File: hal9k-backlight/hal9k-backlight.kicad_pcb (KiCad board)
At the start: 2 copper layers, 76 x 13 mm, 14 parts, among them J1 +, J2 GND, J3 Din, J4 Dout

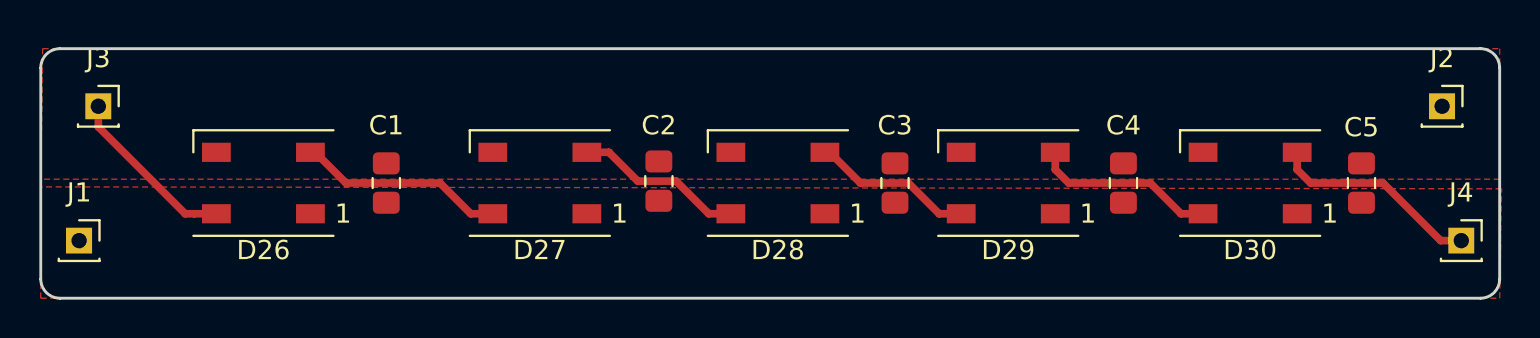
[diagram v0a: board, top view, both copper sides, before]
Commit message: backlight update
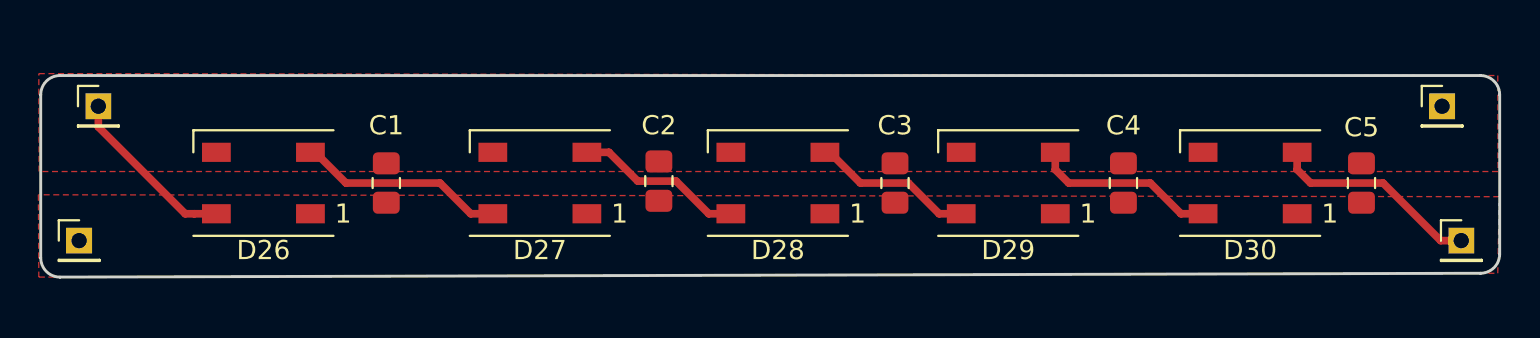
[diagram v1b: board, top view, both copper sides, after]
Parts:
- J1, J2, J3, J4: footprint Connector_PinSocket_2.00mm:PinSocket_1x01_P2.00mm_Vertical -> Connector_PinHeader_2.00mm:PinHeader_1x01_P2.00mm_Vertical
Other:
- board size 76 x 13 mm -> 76 x 10.5 mm
